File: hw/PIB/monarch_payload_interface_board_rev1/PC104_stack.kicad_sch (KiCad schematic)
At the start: 19 parts, among them U1 Payload, U10 AD7124-8BCPZ-RL, U11 WSK06121L000FEA, U12 WSK06121L000FEA, U13 WSK06121L000FEA

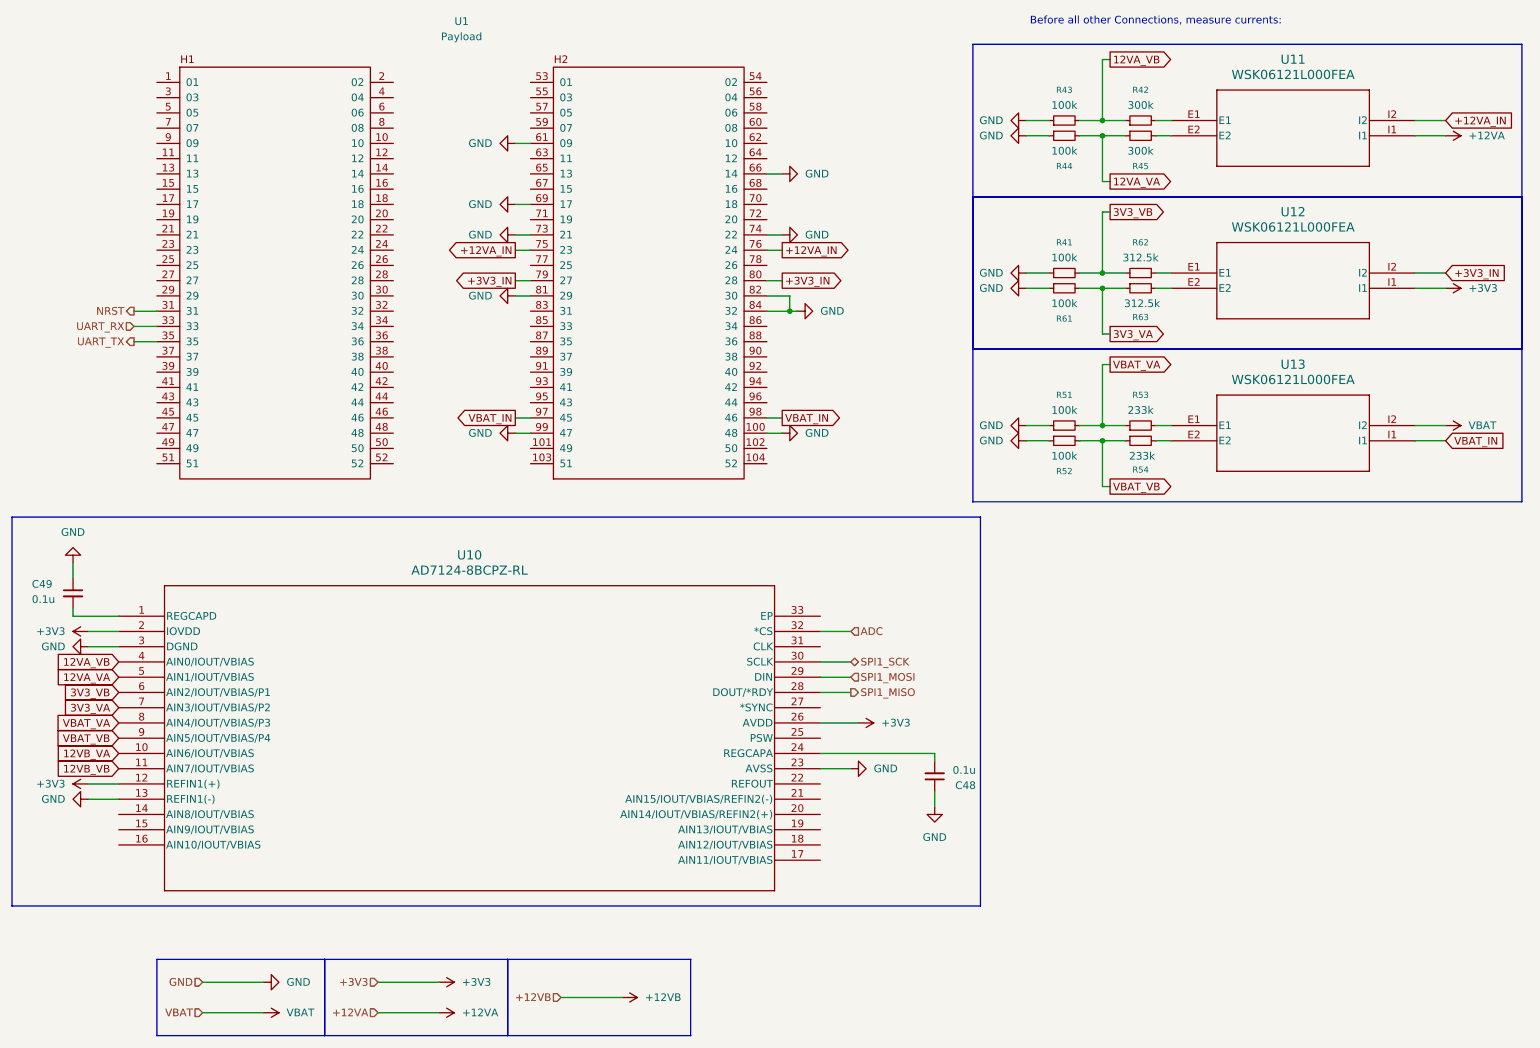
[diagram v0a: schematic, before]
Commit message: PIB layout update
done pending Ben O approval
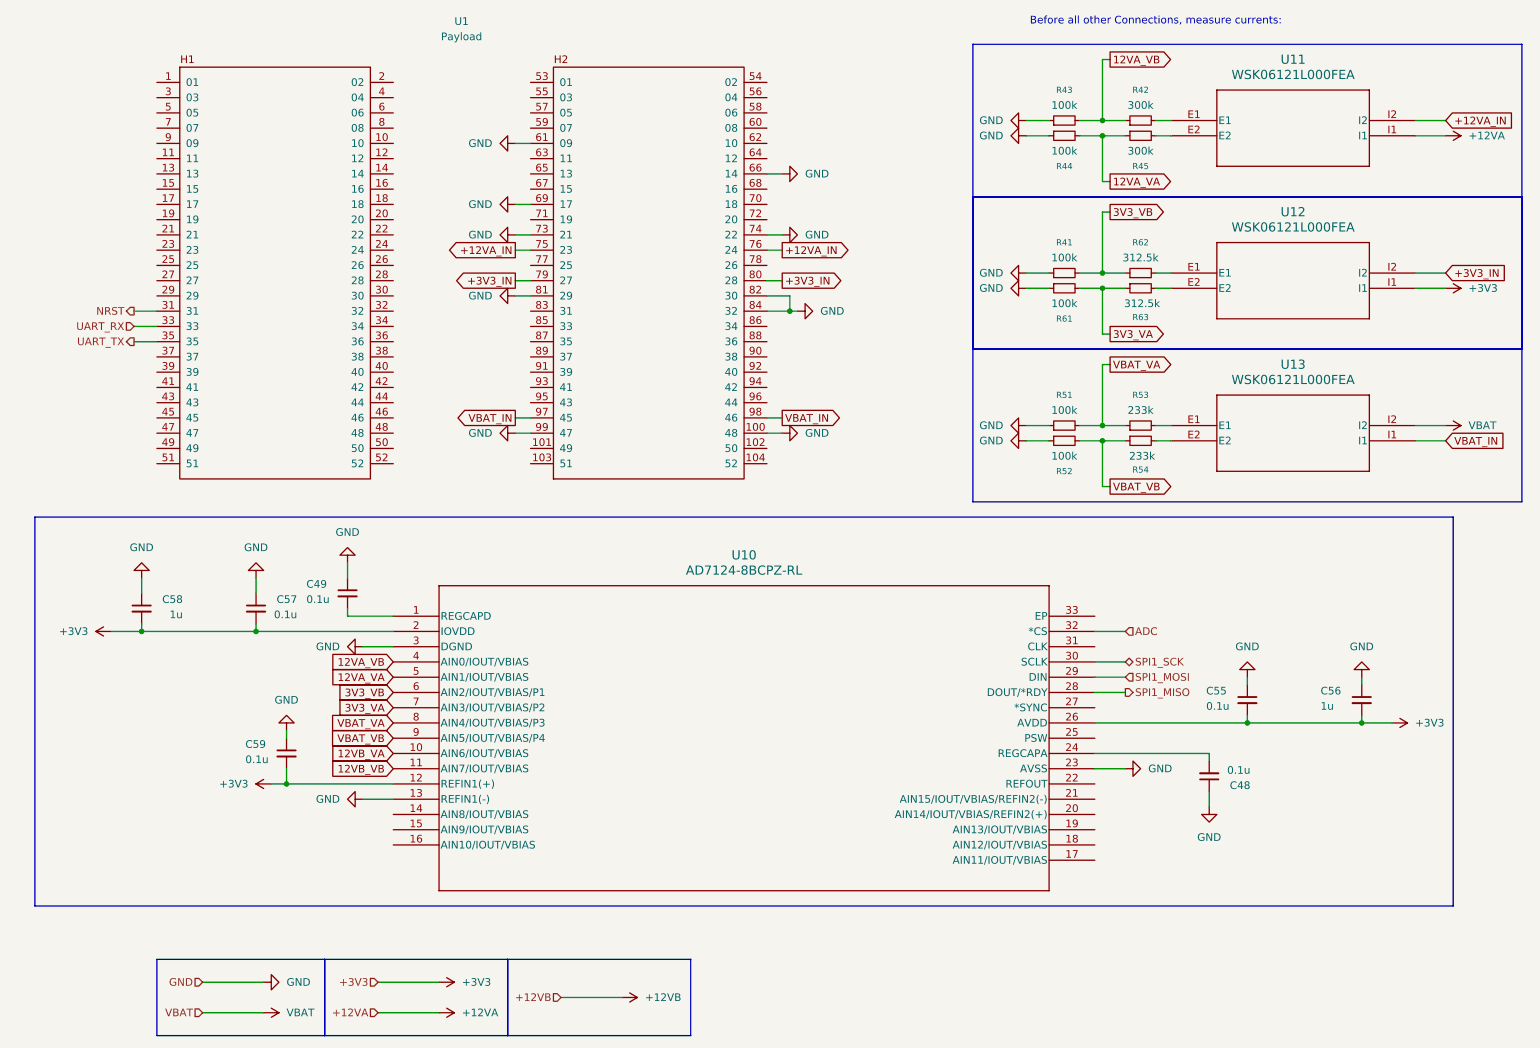
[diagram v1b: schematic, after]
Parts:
- added C55, C57, C59: 0.1u, Capacitor_SMD:C_0603_1608Metric, symbol Device:C_Small
- added C56, C58: 1u, Capacitor_SMD:C_0603_1608Metric, symbol Device:C_Small
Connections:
- net +3V3: now also C55.2, C56.2, C57.2, C58.2, C59.2
- net GND: now also C55.1, C56.1, C57.1, C58.1, C59.1
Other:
- moved on the sheet: C48, C49, U10
